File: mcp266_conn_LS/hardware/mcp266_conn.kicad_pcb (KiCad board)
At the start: 2 copper layers, 83.2 x 40.5 mm, 19 parts, among them J1 conn_dsub_plug_15pos, J10 CAN, J11 CANL jumper, J12 CANH jumper, J2 CAN, J3 LS1, J4 LS2, J5 LS3, J6 LS4, J7 Enc1, J8 Enc2, J9 enc conn

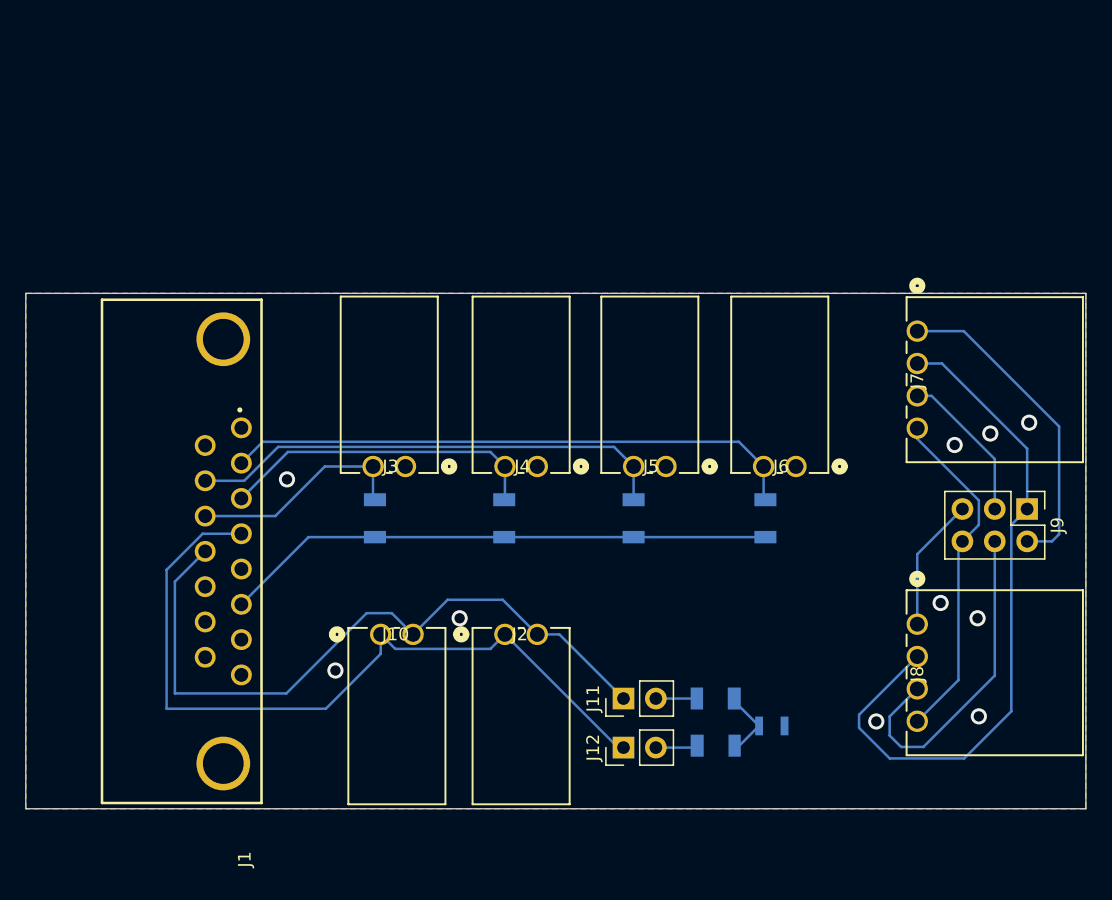
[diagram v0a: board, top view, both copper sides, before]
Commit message: design three seperate mcp connectors that can each dasiy chain for can, and one has limit switch headers and another the can termination
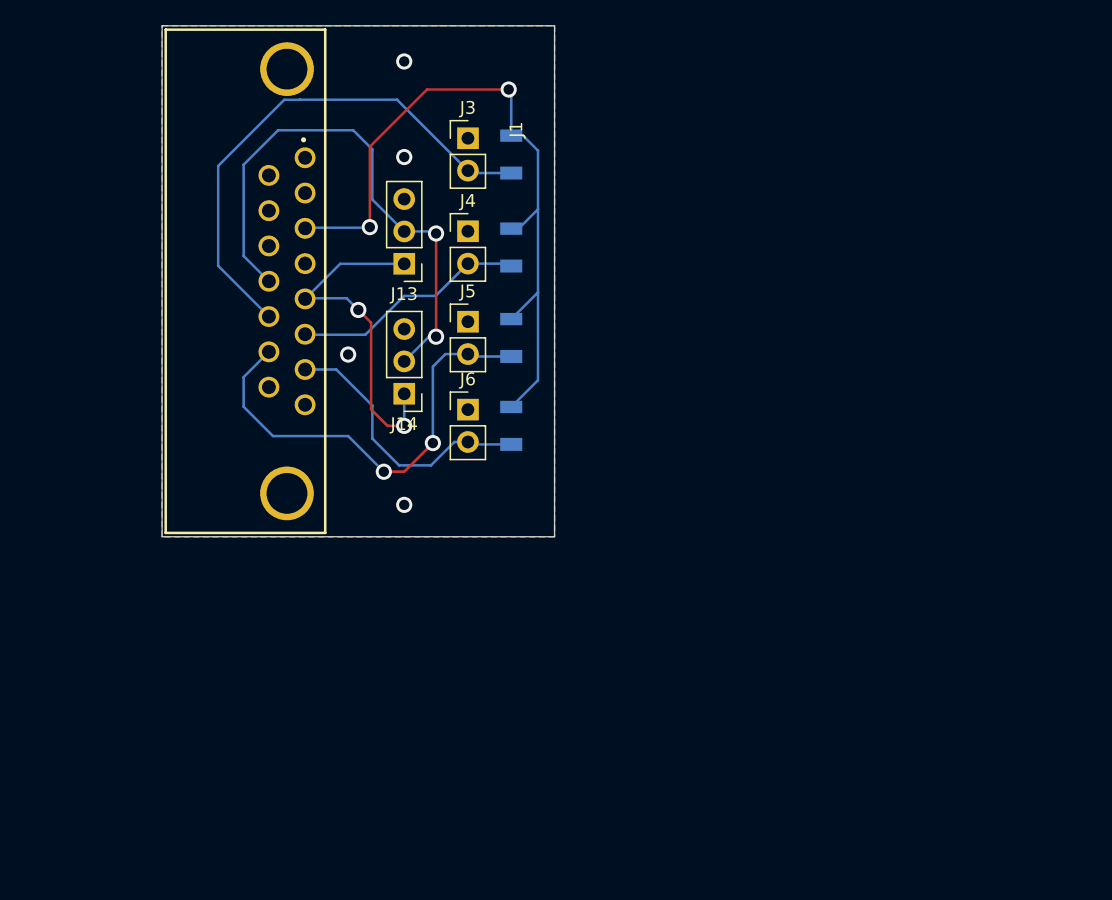
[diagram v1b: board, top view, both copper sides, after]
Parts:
- removed C1: 47nf, mcp266_conn:CAPC2012X145N
- removed J10, J2: CAN, mcp266_conn:HEADER90_2pin
- removed J11: CANL jumper, Connector_PinHeader_2.54mm:PinHeader_1x02_P2.54mm_Vertical
- removed J12: CANH jumper, Connector_PinHeader_2.54mm:PinHeader_1x02_P2.54mm_Vertical
- removed J7: Enc1, mcp266_conn:HEADER90_4pin
- removed J8: Enc2, mcp266_conn:HEADER90_4pin
- removed J9: enc conn, Connector_PinHeader_2.54mm:PinHeader_2x03_P2.54mm_Vertical
- removed R1, R6: 60, mcp266_conn:RESC3116X65N
- added J13: CAN, Connector_PinHeader_2.54mm:PinHeader_1x03_P2.54mm_Vertical, F.Cu at (109.3, 58.4)
- added J14: CAN, Connector_PinHeader_2.54mm:PinHeader_1x03_P2.54mm_Vertical, F.Cu at (109.3, 68.6)
- J3, J4, J5, J6: footprint mcp266_conn:HEADER90_2pin -> Connector_PinHeader_2.54mm:PinHeader_1x02_P2.54mm_Vertical
- moved R2 30.5 mm to (117.7, 49.8), turned to 90 degrees
- moved J3 26.2 mm to (114.3, 48.5), turned to 0 degrees
- moved J6 26.1 mm to (114.3, 69.8), turned to 0 degrees
- moved J1 21.8 mm to (93.8, 59.8)
- moved R3 21.3 mm to (117.7, 57.1), turned to 90 degrees
- moved R5 21.2 mm to (117.7, 71.1), turned to 90 degrees
- moved J5 19.3 mm to (114.3, 62.9), turned to 0 degrees
- moved J4 19.2 mm to (114.3, 55.8), turned to 0 degrees
- moved R4 17.1 mm to (117.7, 64.2), turned to 90 degrees
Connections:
- J1 pad 10: /LS3 -> unconnected-(J1-Pad10)
- J1 pad 11: /LS1 -> unconnected-(J1-Pad11)
- J1 pad 13: unconnected-(J1-Pad13) -> /LS1
- J1 pad 14: unconnected-(J1-Pad14) -> /LS3
- J1 pad 2: /LS4 -> /GND
- J1 pad 3: /LS2 -> /5V
- J1 pad 4: /CANH -> unconnected-(J1-Pad4)
- J1 pad 5: unconnected-(J1-Pad5) -> /CANH
- J1 pad 6: /5V -> /LS2
- J1 pad 7: GND -> /LS4
- J3 pad 1: GND -> /GND
- J4 pad 1: GND -> /GND
- J5 pad 1: GND -> /GND
- J6 pad 1: GND -> /GND
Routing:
- net /5V_enc: track 54.5 -> 0.00 mm
- net /CANH: track 61.7 -> 27.2 mm, vias 0 -> 2
- net /GND_enc: track 27.0 -> 0.00 mm
- net /2B: track 26.0 -> 0.00 mm
- net /1A: track 25.4 -> 0.00 mm
- net /LS1: track 17.4 -> 41.0 mm
- net /LS4: track 44.8 -> 21.7 mm
- net /5V: track 43.4 -> 57.2 mm, vias 0 -> 2
- net /1B: track 12.1 -> 0.00 mm
- net /CANL: track 55.0 -> 43.5 mm, vias 0 -> 2
- net /2A: track 10.5 -> 0.00 mm
- net /LS2: track 25.2 -> 18.6 mm
- net Net-(C1-Pad2): track 5.52 -> 0.00 mm
- net /CANH_1: track 3.31 -> 0.00 mm
- net /CANL_L: track 3.22 -> 0.00 mm
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- added copper zone on B.Cu, net /GND
- added copper zone on F.Cu, net /GND
- removed copper zone on B.Cu, net GND
- removed copper zone on F.Cu, net GND
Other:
- board size 83.2 x 40.5 mm -> 30.8 x 40.1 mm

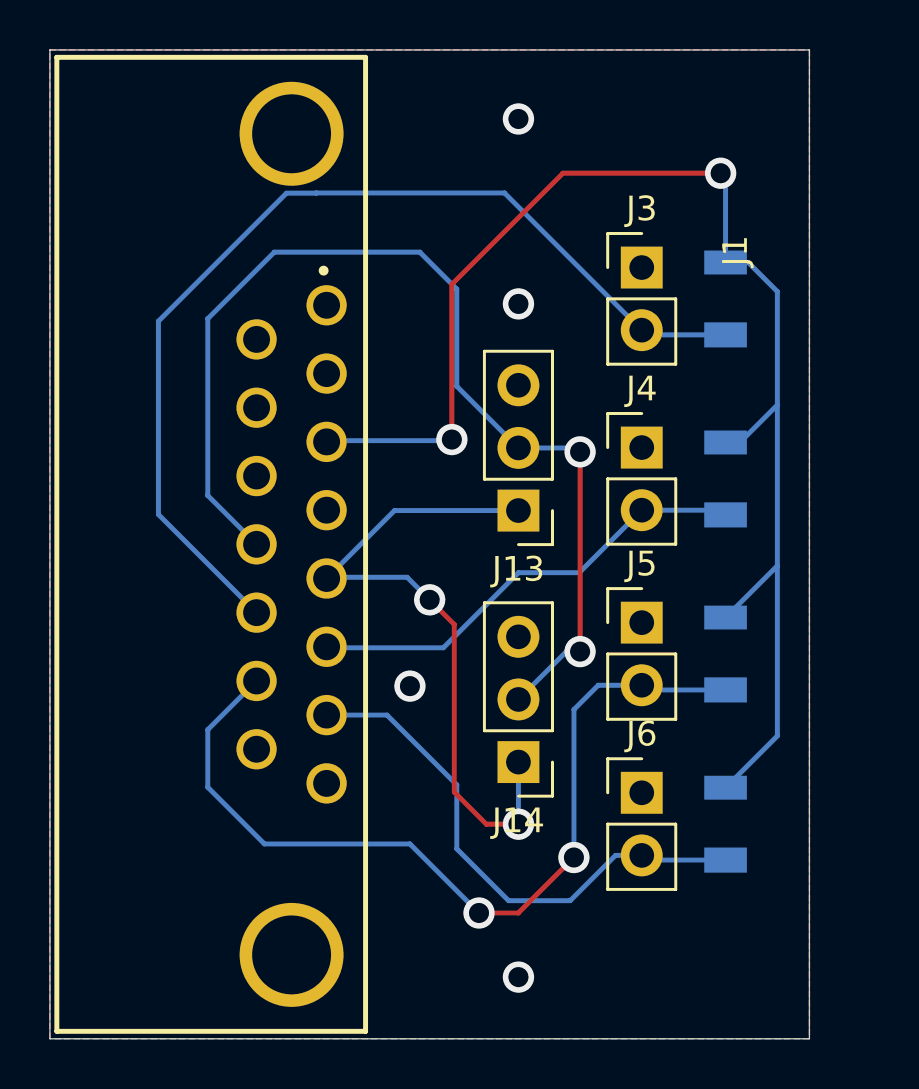
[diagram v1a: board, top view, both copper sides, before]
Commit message: conn for ls designed with jlc parts
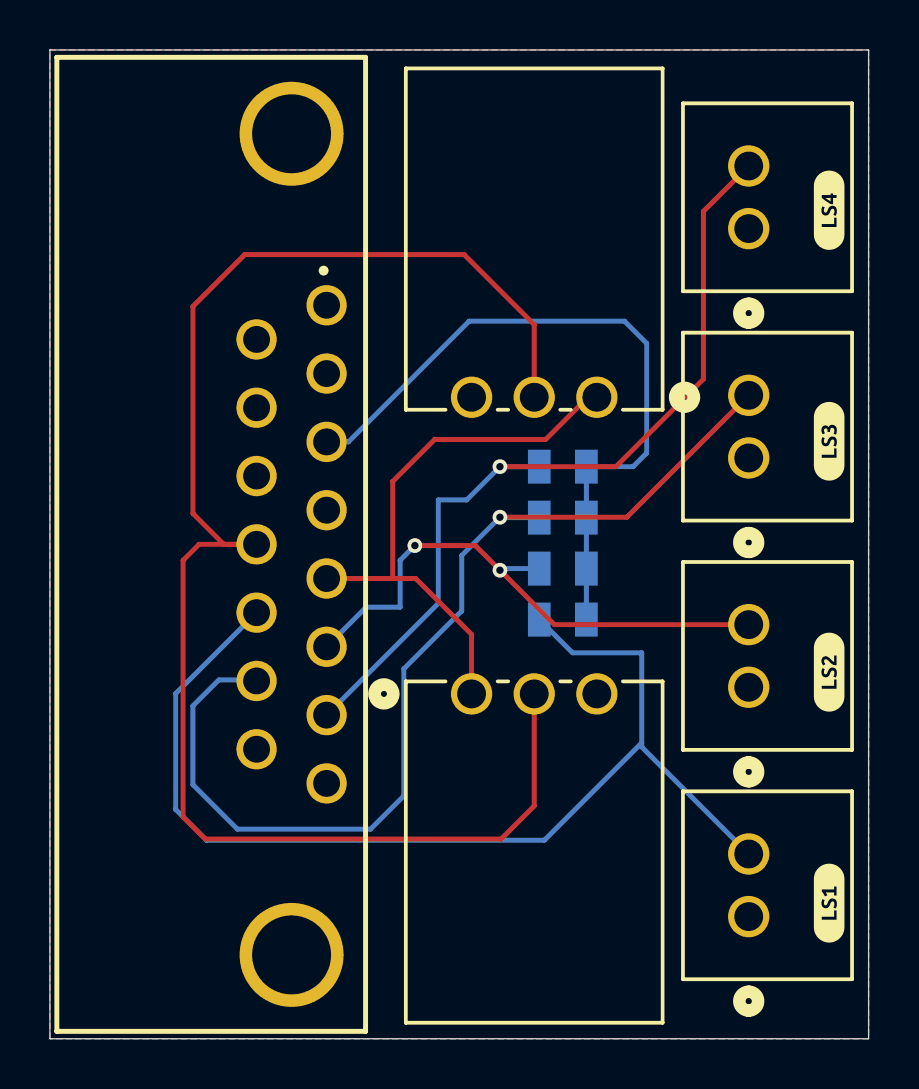
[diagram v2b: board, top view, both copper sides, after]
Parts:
- added kibuzzard-6AD62E2F: G***, kibuzzard-6AD62E2F, F.Cu at (121.9, 74.3)
- added kibuzzard-6AD62EFE: G***, kibuzzard-6AD62EFE, F.Cu at (121.9, 64.9)
- added kibuzzard-6AD62F13: G***, kibuzzard-6AD62F13, F.Cu at (121.9, 55.6)
- added kibuzzard-6AD62F21: G***, kibuzzard-6AD62F21, F.Cu at (121.9, 46.2)
- J1: value conn_dsub_plug_15pos -> 618015211721
- J13, J14: footprint Connector_PinHeader_2.54mm:PinHeader_1x03_P2.54mm_Vertical -> mcp266_conn:HEADER_3pos_90degree
- J3, J4, J5, J6: footprint Connector_PinHeader_2.54mm:PinHeader_1x02_P2.54mm_Vertical -> mcp266_conn:HEADER_2pos
- R2, R3, R4, R5: footprint mcp266_conn:RESC3116X65N -> mcp266_conn:RES_1.2k
- moved J3 26.7 mm to (118.6, 74.8), turned to -90 degrees
- moved J6 23.3 mm to (118.6, 46.9), turned to -90 degrees
- moved R5 15.9 mm to (111.1, 56.6), turned to 0 degrees
- moved R2 14.6 mm to (111.1, 62.8), turned to 0 degrees
- moved J4 10.6 mm to (118.6, 65.5), turned to -90 degrees
- moved R4 8.61 mm to (111.1, 58.7), turned to 0 degrees
- moved J5 7.96 mm to (118.6, 56.2), turned to -90 degrees
- moved R3 7.53 mm to (111.1, 60.7), turned to 0 degrees
- moved J13 5.59 mm to (112.5, 53.8)
- moved J14 3.36 mm to (107.4, 65.8), turned to 0 degrees
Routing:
- net /5V: track 57.2 -> 28.8 mm, vias 2 -> 0
- net /CANL: track 43.5 -> 63.7 mm, vias 2 -> 0
- net /LS4: track 21.7 -> 34.4 mm, vias 0 -> 1
- net /LS3: track 35.7 -> 42.7 mm, vias 2 -> 1
- net /LS2: track 18.6 -> 22.7 mm, vias 0 -> 2
- net /LS1: track 41.0 -> 45.1 mm
- net /CANH: track 27.2 -> 25.5 mm, vias 2 -> 0
- net /GND: vias 4 -> 0
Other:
- board size 30.8 x 40.1 mm -> 33.2 x 40.1 mm
